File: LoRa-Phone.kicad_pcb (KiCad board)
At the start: 4 copper layers, 81.6 x 102.5 mm, 218 parts, among them IC1 SKY13373-460LF, IC10 TPS22965NTDSGRQ1, IC2 AD8318ACPZ-REEL7, IC3 AD8318ACPZ-REEL7, IC4 TPS2121RUXT, IC5 MAX17048G+T10, IC6 MAX17048G+T10, IC7 TCA9543ADR, IC8 MAX16150AUT+T, IC9 SN74LVC1G74RSE2, J1 Interface, J3 Board_1, J4 BUTTON, J4 JST_MAIN, J5 Board_1, J6 ROTARY_ENCODER, M1 Motor_DC, Q1 AO3400A, Q2 AO3400A, Q3 AO3400A, Q4 AO3401A, SW1 POWER, U1 ESP32-S3-WROOM-2, U10 DRV2605LDGS, U11 LC76G, U12 RV-3028-C7, U13 SA818S, U14 INA219BxDCN, U15 INA219BxDCN, U16 INA219BxDCN, U17 MCP4725xxx-xCH, U18 TLV3501AIDBV, U19 RIC11-31S10K2-GSMT, U2 TCD-10-23BDX+, U21 WM8960, U23 E22-900M30S, U24 E22-170M30S, U3 MCP23017x-x-ML, U4 BMP390, U5 IS31FL3218-QF, U6 LSM6DSOXTR, U7 BQ24075RGT, U8 MCP23017x-x-ML, U9 BQ24075RGT

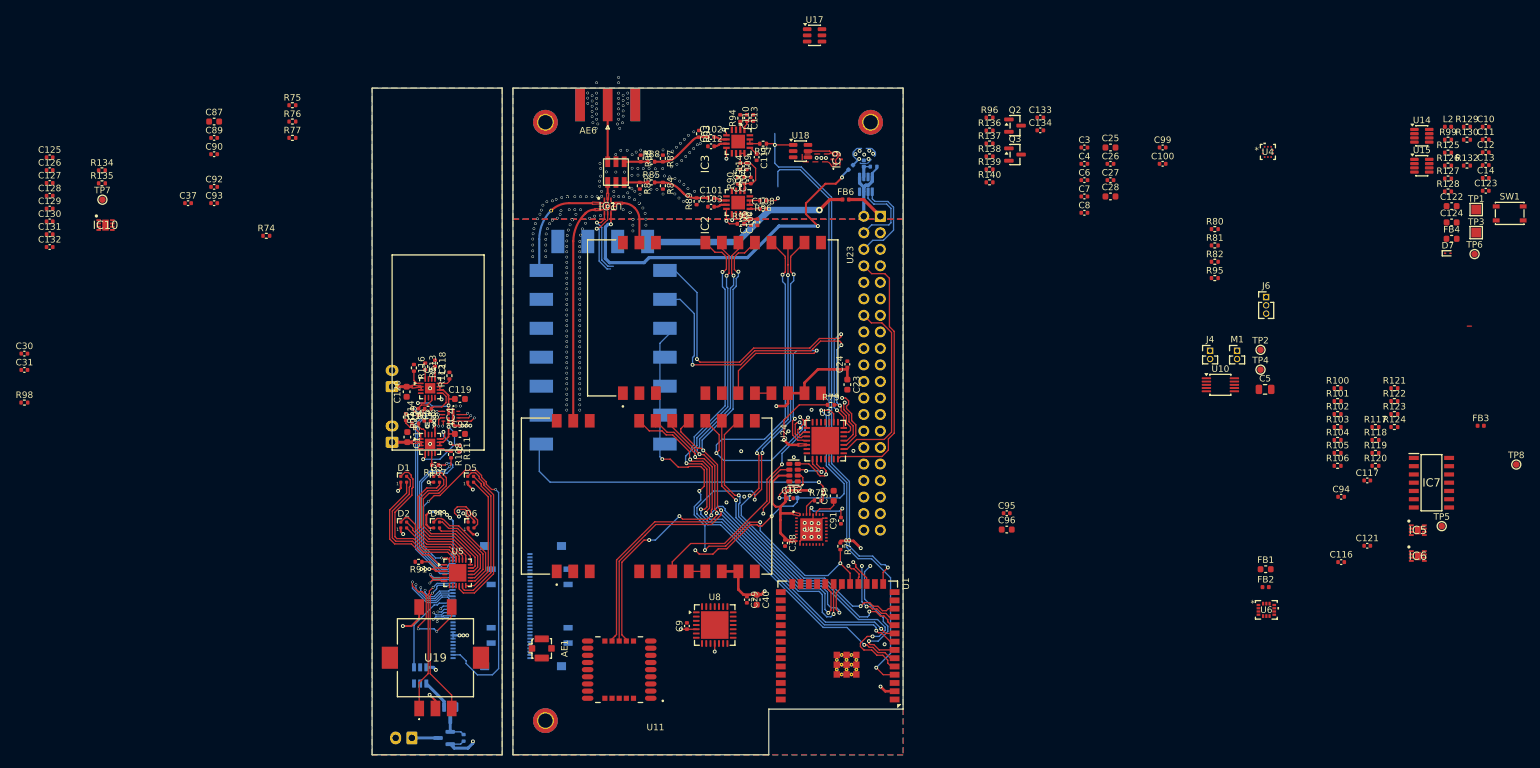
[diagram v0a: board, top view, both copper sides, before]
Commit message: Finished routing main PCB
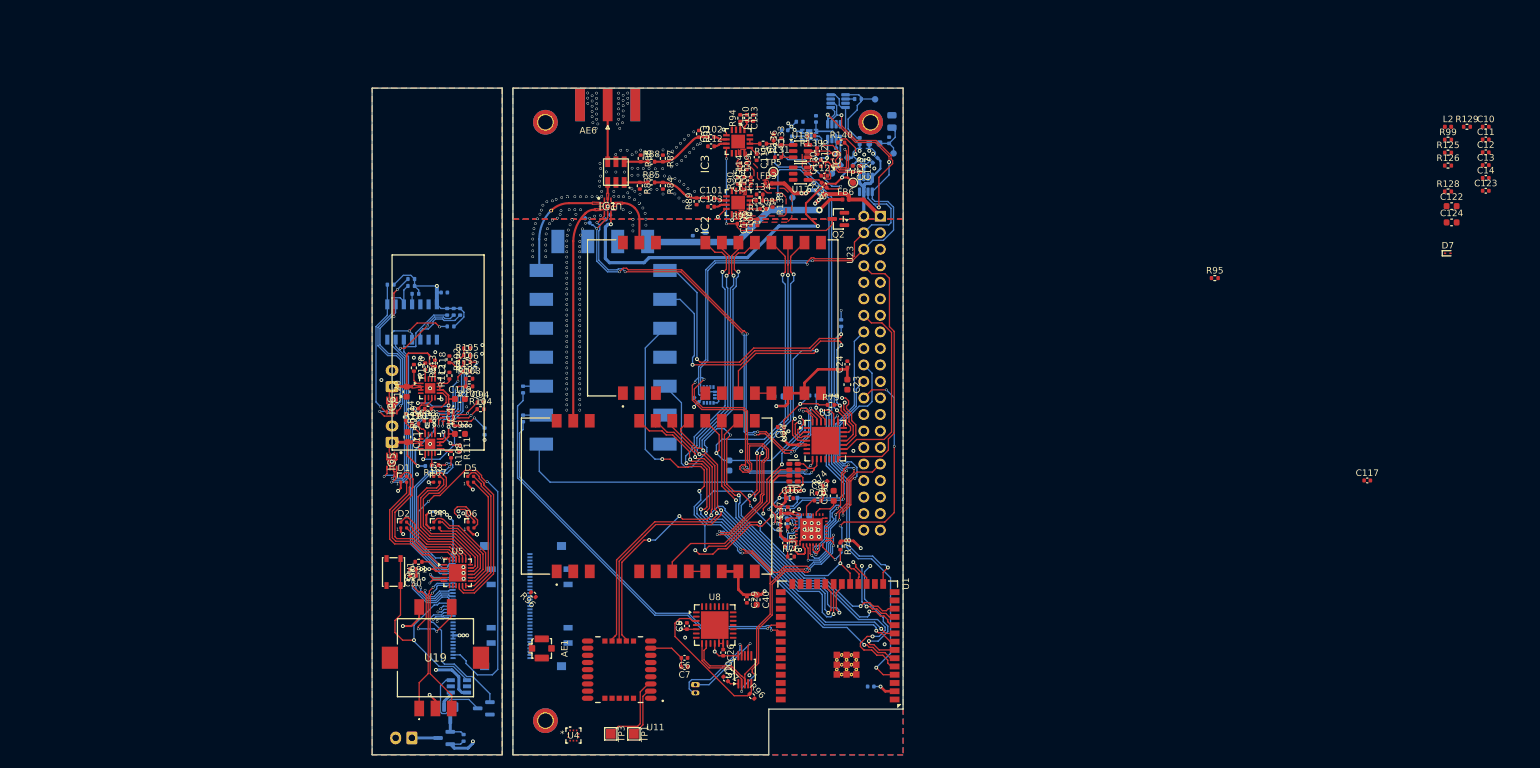
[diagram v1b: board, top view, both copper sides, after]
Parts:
- removed C129: 2.2uF, Capacitor_SMD:C_0402_1005Metric
- removed C91, C92: 100nF, Capacitor_SMD:C_0402_1005Metric
- removed the J4 at (223.8, 91.6)
- removed J6: ROTARY_ENCODER, Connector_PinHeader_1.27mm:PinHeader_1x03_P1.27mm_Vertical
- added C135: 100nF, Capacitor_SMD:C_0402_1005Metric, B.Cu at (163.2, 56.0)
- added C136: 22uF, Capacitor_SMD:C_0402_1005Metric, B.Cu at (158.4, 57.7)
- added C137: 100nF, Capacitor_SMD:C_0402_1005Metric, B.Cu at (144.8, 99.2)
- added R141: 3.3K, Resistor_SMD:R_0402_1005Metric, B.Cu at (160.7, 56.4)
- C100, C116, C121, C132, C25, C28, C3, C4, C5, C87, C90, C93, C95, C96, C99, FB1, FB2, FB4, IC10, IC7, Q3, R117, R118, R119, R120, R121, R122, R123, R124, R127, R130, R134, R77, R80, R81, R82, R98, TP2, TP4, TP6, TP8, U14, U15, U6: moved to B.Cu
- M1: footprint Connector_PinHeader_1.27mm:PinHeader_1x02_P1.27mm_Vertical -> Connector_Molex:Molex_PicoBlade_53048-0210_1x02_P1.25mm_Horizontal; moved to B.Cu
- moved SW1 180.3 mm to (98.2, 125.7), turned to -90 degrees
- moved IC6 159.4 mm to (98.0, 100.0), turned to -90 degrees
- moved IC7 158.7 mm to (101.1, 87.2), turned to 90 degrees
- moved IC5 158.1 mm to (98.0, 108.7), turned to -90 degrees
- moved R132 157.0 mm to (109.5, 94.8)
- moved TP3 153.8 mm to (131.7, 150.5), turned to -90 degrees
- moved R119 153.6 mm to (97.8, 81.5)
- moved TP1 152.5 mm to (135.2, 150.5), turned to -90 degrees
- moved R124 151.9 mm to (101.6, 82.9)
- moved R118 150.3 mm to (101.0, 80.6)
- moved R117 149.8 mm to (101.0, 81.7)
- moved C121 147.2 mm to (106.0, 82.7), turned to 180 degrees
- moved R121 146.1 mm to (106.5, 85.6), turned to 90 degrees
- moved R122 145.3 mm to (107.5, 85.6), turned to 90 degrees
- moved R123 144.5 mm to (108.5, 85.6), turned to 90 degrees
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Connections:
- C118 pad 2: +5V -> BAT2
- C98 pad 2: +5V -> BAT1
- J5 pad 25: +5V -> +5V_B
- J5 pad 26: +5V -> +5V_B
- J5 pad 27: +5V -> +5V_B
- U13 pad 1: AUDIO_ON -> unconnected-(U13-AUDIO_ON-Pad1)
- U21 pad 29: Net-(U21-HEADPHONE_R) -> unconnected-(U21-HEADPHONE_R-Pad29)
- U21 pad 31: Net-(U21-HEADPHONE_L) -> unconnected-(U21-HEADPHONE_L-Pad31)
- U3 pad 1: MOTOR -> unconnected-(U3-GPB4-Pad1)
- U3 pad 19: SDB_1 -> unconnected-(U3-GPA2-Pad19)
- U3 pad 25: unconnected-(U3-GPB0-Pad25) -> SDB_1
- U7 pad 13: +5V -> BAT1
- U8 pad 3: unconnected-(U8-GPB6-Pad3) -> MOTOR
- U9 pad 13: +5V -> BAT2
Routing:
- net +3V3: track 77.8 -> 312.3 mm, vias 32 -> 37
- net SCL: track 20.6 -> 207.6 mm, vias 2 -> 13
- net SDA: track 20.7 -> 202.7 mm, vias 1 -> 10
- net +3V3_RADIO: track 26.6 -> 108.4 mm, vias 2 -> 5
- net Net-(U1-IO38): track 0.00 -> 63.7 mm, vias 0 -> 1
- net RFS_V1: track 10.6 -> 73.7 mm, vias 1 -> 6
- net RFS_V2: track 10.8 -> 72.1 mm, vias 1 -> 6
- net Net-(U1-MTCK/IO39): track 0.00 -> 59.2 mm, vias 0 -> 1
- net LINPUT1: track 0.00 -> 46.1 mm, vias 0 -> 2
- net WM8960_DAC/ADC_LRC: track 0.00 -> 44.8 mm, vias 0 -> 3
- net WM8960_BLCK: track 0.00 -> 44.2 mm, vias 0 -> 3
- net WM8960_ACDDAT: track 0.00 -> 41.3 mm, vias 0 -> 4
- net BAT1_INT: track 0.00 -> 38.7 mm, vias 0 -> 3
- net SC0: track 0.00 -> 37.0 mm, vias 0 -> 3
- net SD0: track 0.00 -> 36.8 mm, vias 0 -> 1
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- added copper zone on F.Cu, net +5V_RF

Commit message: Routed all PCB, missing antenna variable capacitors
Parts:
- removed C10, C14: 100pF, Capacitor_SMD:C_0402_1005Metric
- removed C11, C12: NC, Capacitor_SMD:C_0402_1005Metric
- removed C13, C6: 100nF, Capacitor_SMD:C_0402_1005Metric
- removed C7: 10uF, Capacitor_SMD:C_0402_1005Metric
- removed D7: D_TVS, Diode_SMD:D_SOD-923
- removed L2: 68nH, Inductor_SMD:L_0402_1005Metric
- removed R125: 0R, Resistor_SMD:R_0402_1005Metric
- removed R126: 10R, Resistor_SMD:R_0402_1005Metric
- removed R99: 10K, Resistor_SMD:R_0402_1005Metric
- removed U11: LC76G, PTCR:XCVR_LC76G
- added J2: Joystick, Connector_FFC-FPC:Amphenol_F32Q-1A7x1-11004_1x04-1MP_P0.5mm_Horizontal, F.Cu at (105.0, 83.0)
- added J6: Board_1, Connector_FFC-FPC:Molex_502244-3330_1x33-1MP_P0.5mm_Horizontal, B.Cu at (122.3, 130.9)
- C122, C124: footprint Capacitor_SMD:C_0603_1608Metric -> Capacitor_SMD:C_0402_1005Metric
- C123, R128, R129, TP1, TP3: moved to B.Cu
- J3: value Board_1 -> L76K; footprint Connector_FFC-FPC:Molex_502244-3330_1x33-1MP_P0.5mm_Horizontal -> PTCR:JST_SM08B-SRSS-TB_LF__SN_
- moved R129 179.1 mm to (100.9, 132.8), turned to 180 degrees
- moved C123 175.7 mm to (110.1, 147.8), turned to 180 degrees
- moved R128 167.7 mm to (111.2, 143.9), turned to -90 degrees
- moved C117 152.5 mm to (96.1, 97.7), turned to 90 degrees
- moved C122 110.5 mm to (157.9, 109.5), turned to 90 degrees
- moved C124 110.3 mm to (157.9, 111.3), turned to -90 degrees
- moved TP1 100.5 mm to (161.5, 53.5), turned to 90 degrees
- moved TP3 100.5 mm to (158.0, 53.5), turned to 90 degrees
- moved J3 80.6 mm to (151.1, 55.5), turned to 0 degrees
- moved R95 66.0 mm to (165.7, 110.3), turned to 180 degrees
- moved TP8 5.56 mm to (154.1, 69.3)
- moved U19 0.27 mm to (105.0, 138.8)
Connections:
- D8 pad 2: POWER_BTN_B -> POWER_BTN
- IC8 pad 1: POWER_BTN_B -> POWER_BTN
- J3 pad 1: +3V3 -> GND
- J3 pad 2: +3V3 -> GNSS_CTRL
- J3 pad 3: +3V3 -> +3V3_GNSS
- J3 pad 4: BAT1_PGOOD_1 -> GNSS_TX
- J3 pad 5: BAT1_CHG_1 -> GNSS_RX
- J3 pad 6: BAT2_PGOOD_1 -> GNSS_WAKE
- J3 pad 7: BAT2_CHG_1 -> unconnected-(J3-Pin_7-Pad7)
- J3 pad 8: SDA -> G_RESET
- J5 pad 16: POWER_BTN_B -> POWER_BTN
- R129 pad 1: POWER_BTN_B -> POWER_BTN
- SW1 pad 1: POWER_BTN_B -> POWER_BTN
- TP1 pad 1: Net-(U11-TXD) -> GNSS_RX
- TP3 pad 1: Net-(U11-RXD) -> GNSS_TX
- U1 pad 34: unconnected-(U1-MTDI/IO41-Pad34) -> GNSS_RX
- U1 pad 35: CS_GNSS -> GNSS_TX
- U3 pad 19: unconnected-(U3-GPA2-Pad19) -> GNSS_CTRL
- U3 pad 24: unconnected-(U3-GPA7-Pad24) -> GNSS_WAKE
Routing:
- net GNSS_RX: track 0.00 -> 153.0 mm, vias 0 -> 3
- net GNSS_TX: track 0.00 -> 142.0 mm, vias 0 -> 3
- net GNSS_CTRL: track 0.00 -> 74.9 mm, vias 0 -> 5
- net +3V3: track 312.3 -> 242.3 mm, vias 37 -> 36
- net BATS_INT: track 3.71 -> 72.5 mm, vias 1 -> 4
- net BATS_RESET: track 11.8 -> 74.2 mm, vias 1 -> 8
- net GNSS_WAKE: track 0.00 -> 62.1 mm, vias 0 -> 3
- net JOYSTICK_Y_B: track 6.34 -> 61.8 mm
- net JOYSTICK_X_B: track 5.36 -> 59.9 mm
- net BAT_SEL: track 12.4 -> 54.5 mm
- net POWER_BTN: track 45.2 -> 82.4 mm, vias 3 -> 4
- net POWER_BTN_B: track 35.7 -> 0.00 mm, vias 1 -> 0
- net BAT_VAL: track 8.17 -> 39.9 mm
- net MISO: track 115.1 -> 83.5 mm
- net MOSI: track 115.2 -> 83.8 mm
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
